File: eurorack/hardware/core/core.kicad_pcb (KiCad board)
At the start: 4 copper layers, 19.3 x 69.8 mm, 48 parts, among them J1 ConnNW, J2 ConnSW, J3 ConnNE, J4 ConnSE, J5 Power, J6 SWD, SW1 Reset, SW2 Boot0, U1 STM32F427VGT6, U2 TLV320AIC23BPW, U3 LM1117F-3.3, U4 LM4040C10IDBZR, Y1 Crystal

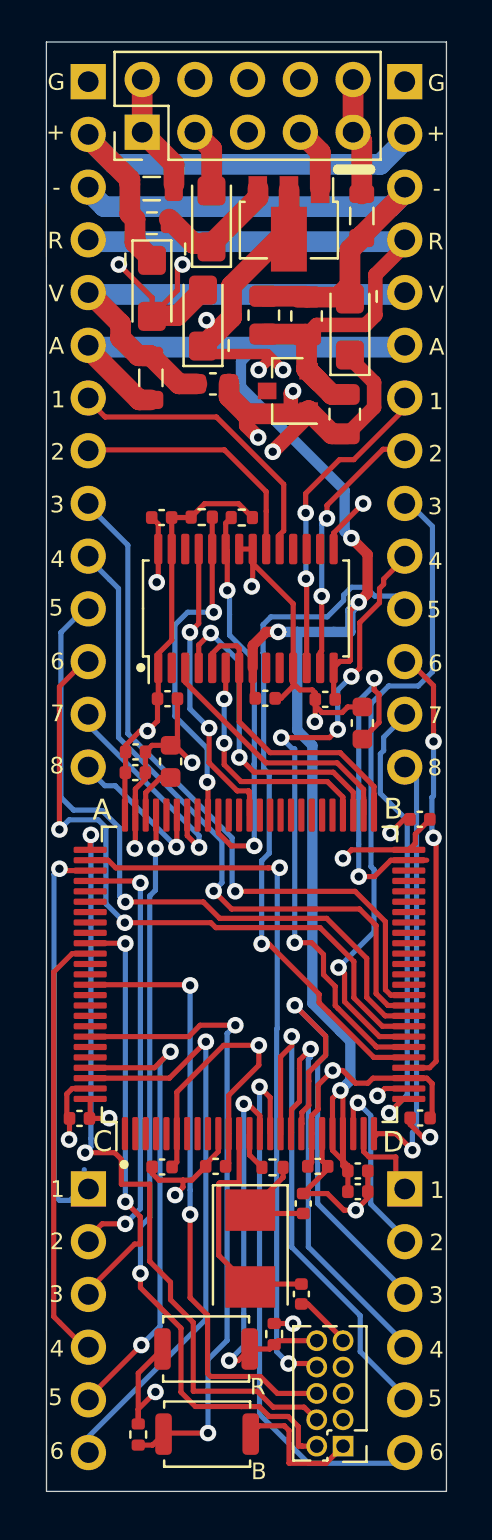
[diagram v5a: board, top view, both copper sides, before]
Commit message: Add protective diodes
Signed-off-by: Petr Horacek <hrck@protonmail.com>
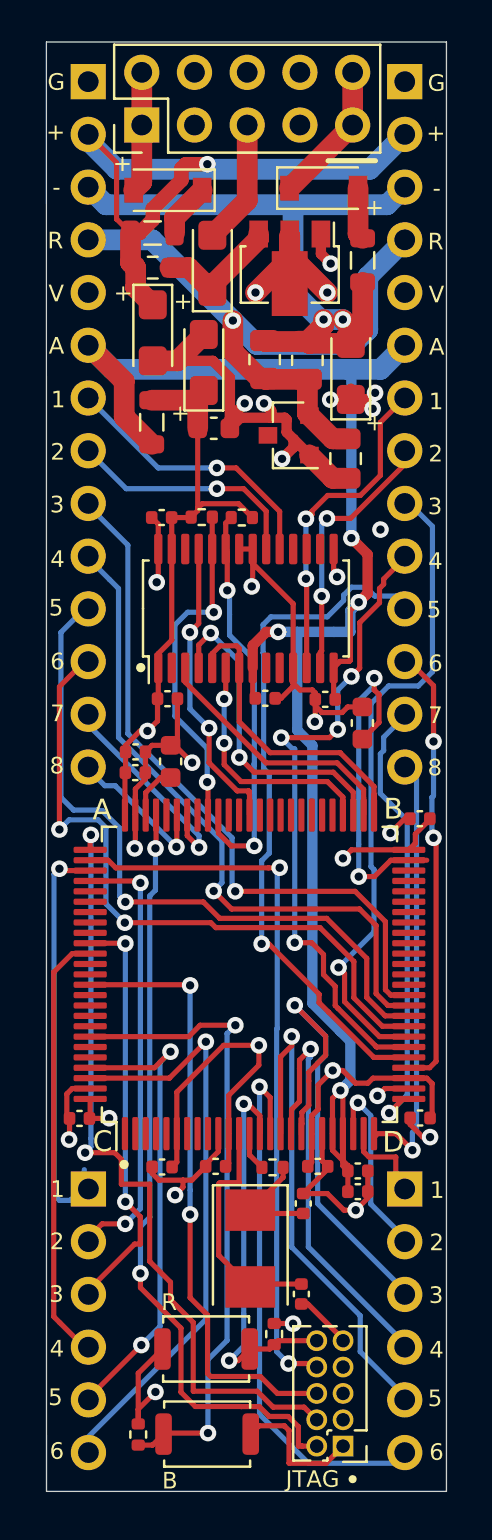
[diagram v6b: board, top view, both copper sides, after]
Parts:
- added D1: D_Small, Diode_SMD:D_SOD-123, F.Cu at (146.6, 72.2)
- added D2: D_Small, Diode_SMD:D_SOD-123, F.Cu at (154.1, 72.1)
- moved C5 2.14 mm to (148.7, 75.7)
- moved C6 2.14 mm to (148.3, 80.5)
- moved FB1 2.14 mm to (145.9, 74.2)
- moved C24 2.14 mm to (155.2, 85.1)
- moved C7 2.14 mm to (148.8, 83.6)
- moved C8 2.14 mm to (145.9, 79.0)
- moved C9 2.14 mm to (155.4, 80.9)
- moved FB2 2.14 mm to (156.0, 75.5)
- moved FB3 2.14 mm to (145.8, 83.3)
- moved R4 2.14 mm to (145.9, 75.9)
- moved R7 2.14 mm to (151.3, 80.3)
- moved R8 2.14 mm to (153.3, 80.4)
- moved U3 2.14 mm to (152.5, 75.9)
- moved U4 2.14 mm to (152.4, 84.0)
- moved J5 0.35 mm to (145.3, 69.0)
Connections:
- FB1 pad 1: Net-(FB1-Pad1) -> Net-(D1-Pad1)
- FB2 pad 1: Net-(FB2-Pad1) -> Net-(D2-Pad2)
- J5 pad 1: Net-(FB1-Pad1) -> Net-(D1-Pad2)
- J5 pad 10: Net-(FB2-Pad1) -> Net-(D2-Pad1)
- J5 pad 2: Net-(FB1-Pad1) -> Net-(D1-Pad2)
- J5 pad 9: Net-(FB2-Pad1) -> Net-(D2-Pad1)
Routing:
- net GND: track 158.3 -> 189.4 mm, vias 18 -> 21
- net +3V3: track 101.3 -> 77.7 mm, vias 9 -> 8
- net VCC: track 23.9 -> 32.0 mm, vias 0 -> 1
- net Net-(D2-Pad1): track 0.00 -> 6.84 mm
- net VEE: track 26.4 -> 33.2 mm, vias 0 -> 2
- net Net-(FB1-Pad1): track 5.69 -> 0.00 mm
- net Net-(FB2-Pad1): track 5.69 -> 0.00 mm
- net Net-(D1-Pad2): track 0.00 -> 5.38 mm
- net Net-(D1-Pad1): track 0.00 -> 2.61 mm
- net Net-(D2-Pad2): track 0.00 -> 2.51 mm
- net +3.3VA: track 84.6 -> 83.2 mm
- net RIN: track 14.5 -> 13.3 mm, vias 0 -> 1
- net LIN: track 12.3 -> 11.6 mm, vias 0 -> 1
- net -10V: track 30.3 -> 30.6 mm, vias 0 -> 1
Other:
- board text added: "JTAG"

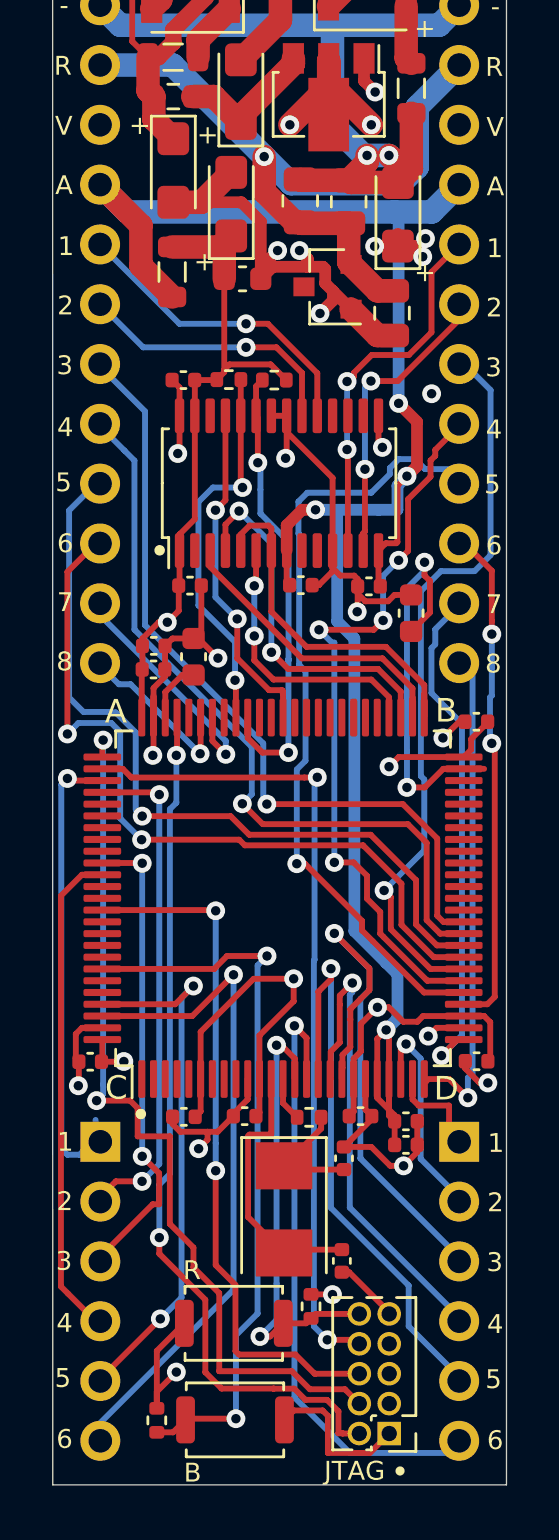
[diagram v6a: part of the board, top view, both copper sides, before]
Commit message: Add mounting holes
Signed-off-by: Petr Horacek <hrck@protonmail.com>
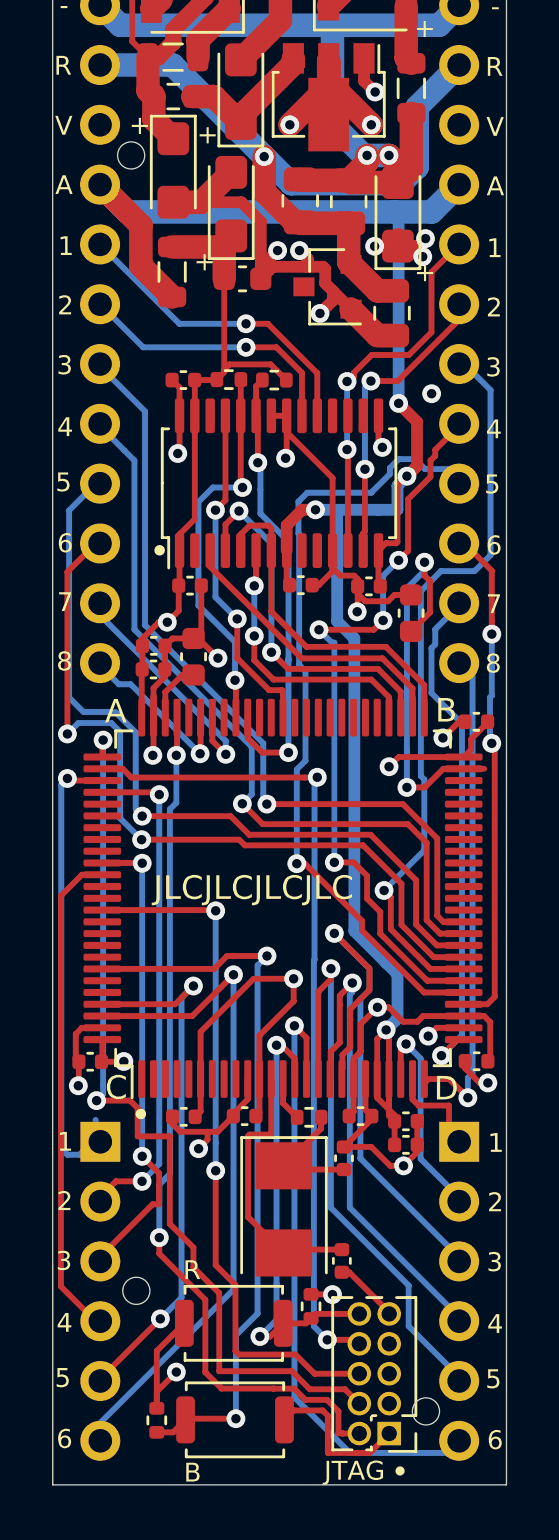
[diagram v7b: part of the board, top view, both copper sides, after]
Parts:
- added REF**: OSHW-Symbol_6.7x6mm_SilkScreen, Symbol:OSHW-Symbol_6.7x6mm_SilkScreen, B.Cu at (150.5, 74.6)
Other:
- outline, holes or cut-outs redrawn
- board text added: "JLCJLCJLCJLC"
- board text added: "cc-by-sa"
- board text added: "rev 1"
